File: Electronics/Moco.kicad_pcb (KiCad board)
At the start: 2 copper layers, 34 x 34 mm, 56 parts, among them J3 USB_C_Receptacle_USB2.0, J4 Conn_01x03, J6 Conn_01x04, J8 Conn_01x01, J9 Conn_01x01, U1 ESP32-C3, U2 TPS562201, U3 TMAG5273, U4 DRV8311, U5 TJA1462ATK/0Z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

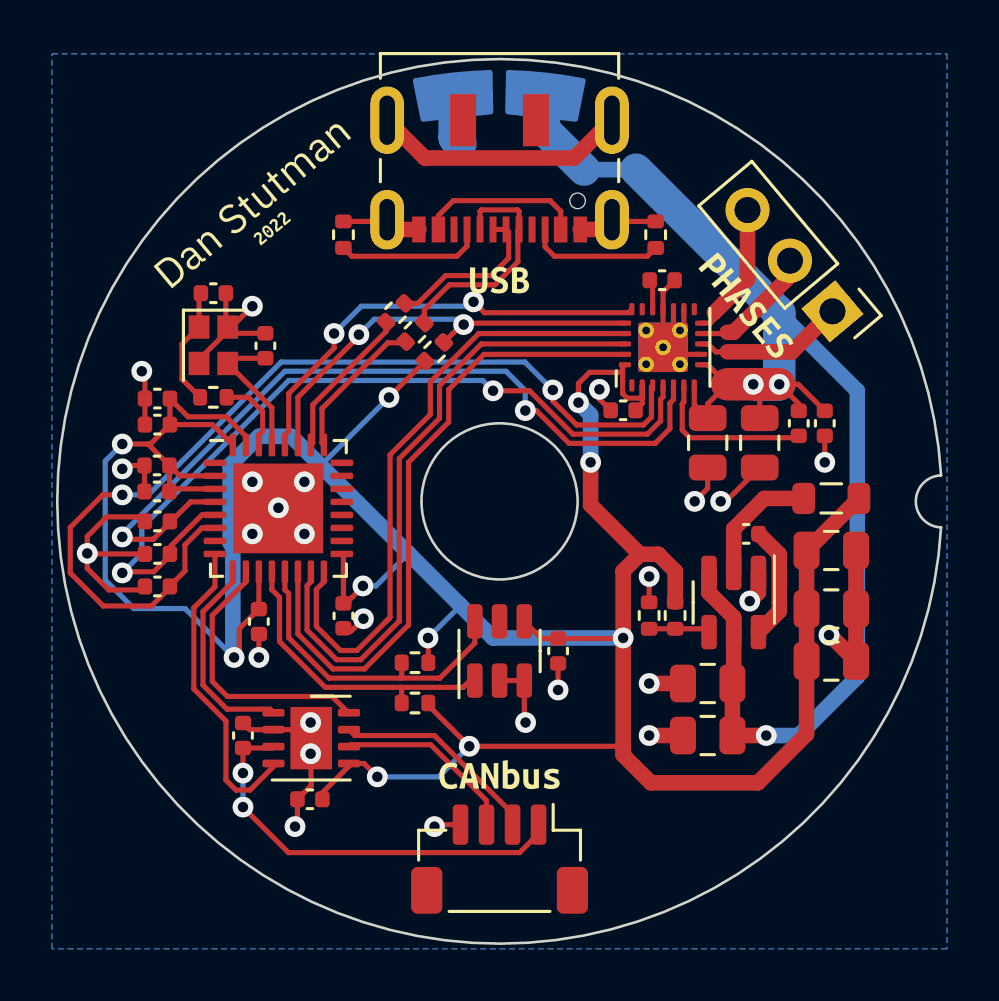
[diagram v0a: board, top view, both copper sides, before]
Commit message: Correct I2C net labels, add NRESET pad
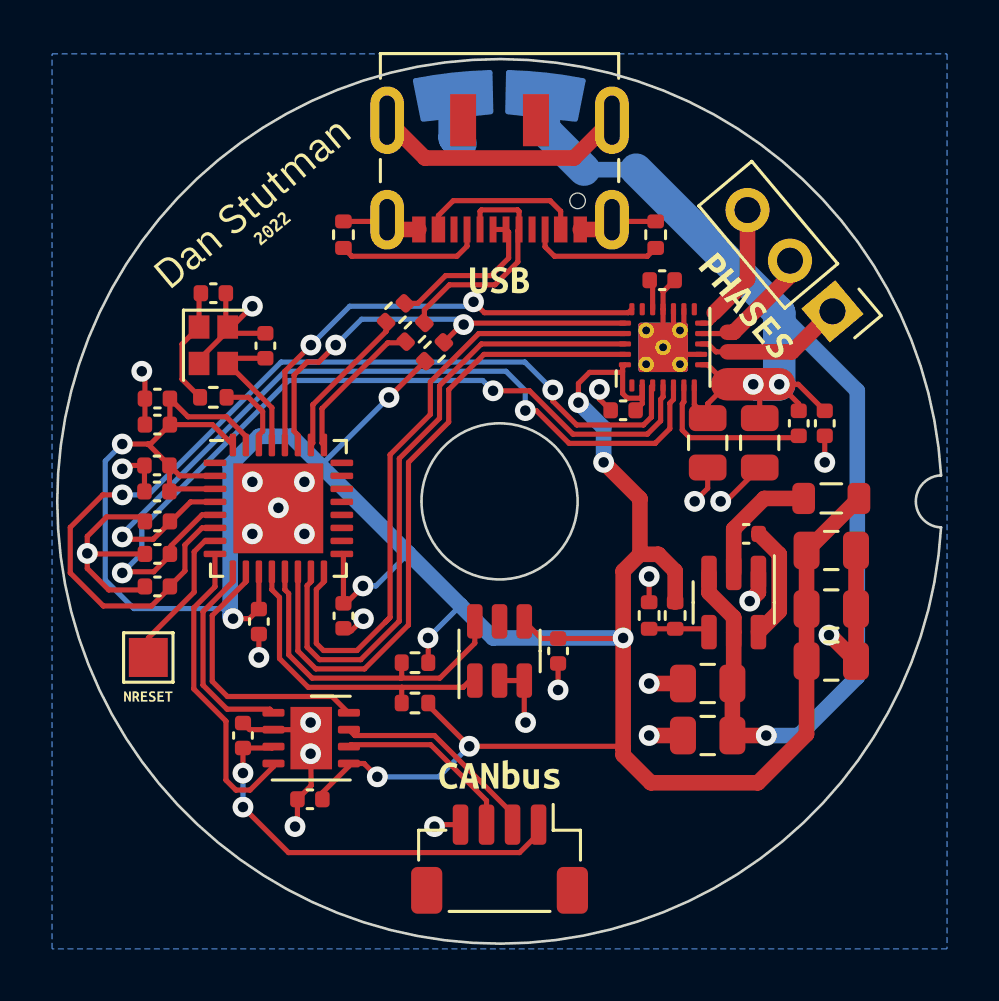
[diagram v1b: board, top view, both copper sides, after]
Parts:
- added TP1: TestPoint, TestPoint:TestPoint_Pad_1.5x1.5mm, F.Cu at (36.5, 56.0)
- added kibuzzard-627B83F7: G***, kibuzzard-627B83F7, F.Cu at (36.5, 57.5)
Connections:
- R1 pad 1: /TMS_SCL -> /TMS_SDA
- R2 pad 2: /TMS_SDA -> /TMS_SCL
- U1 pad 12: /TMS_SDA -> /TMS_SCL
- U1 pad 13: /TMS_SCL -> /TMS_SDA
- U3 pad 1: /TMS_SDA -> /TMS_SCL
- U3 pad 6: /TMS_SCL -> /TMS_SDA
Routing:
- net /~{RESET}: track 0.00 -> 5.77 mm
- net +3V3: track 132.1 -> 129.2 mm
- net /TMS_SDA: track 11.8 -> 12.8 mm
- net /DRV_~{SCS}: track 16.8 -> 17.5 mm
